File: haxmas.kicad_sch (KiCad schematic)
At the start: 13 parts, among them J1 edge +, J2 b-, J3 edge -, J4 b+, J5 back edge +, J6 back edge -

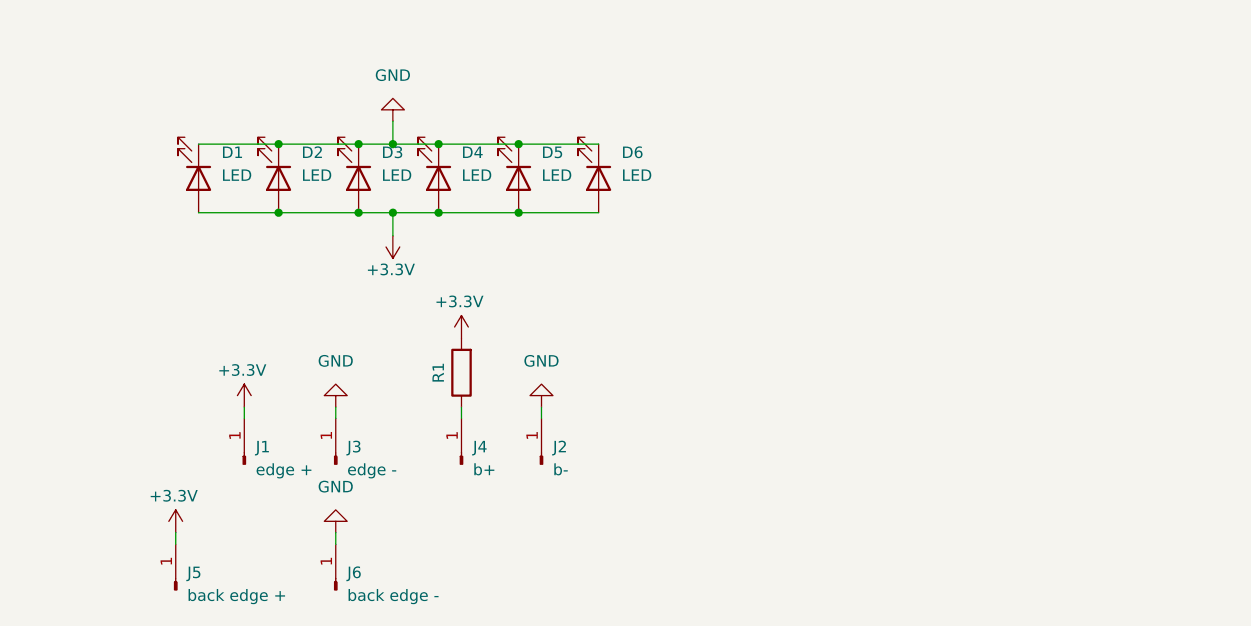
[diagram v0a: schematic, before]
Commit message: feat: add large version
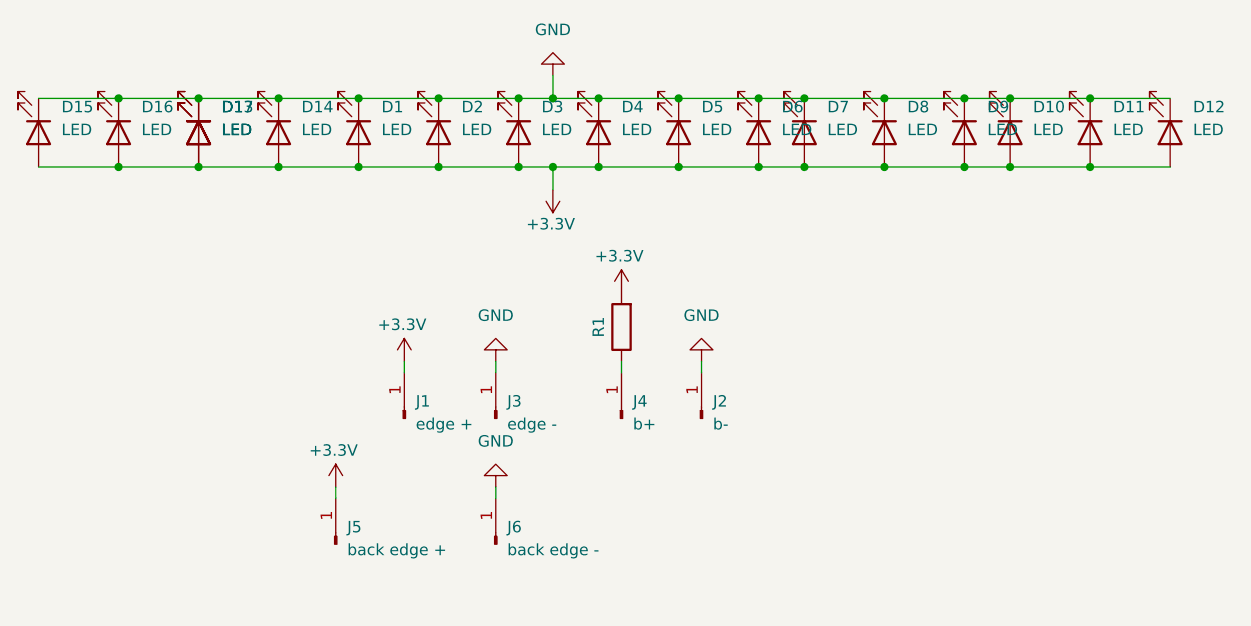
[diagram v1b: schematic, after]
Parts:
- added D10, D11, D12, D13, D14, D15, D16, D17, D7, D8, D9: LED, LED_THT:LED_D3.0mm, symbol Device:LED
- D1, D2, D3, D4, D5, D6: footprint LED_THT:LED_D1.8mm_W3.3mm_H2.4mm -> LED_THT:LED_D3.0mm
- J1, J2, J3, J4, J5, J6: footprint Connector_Wire:SolderWirePad_1x01_SMD_1x2mm -> Connector_Wire:SolderWirePad_1x01_SMD_2x4mm
- R1: footprint Resistor_THT:R_Axial_DIN0204_L3.6mm_D1.6mm_P5.08mm_Horizontal -> Resistor_THT:R_Axial_DIN0204_L3.6mm_D1.6mm_P7.62mm_Horizontal
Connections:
- net +3.3V: now also D10.2 (A), D11.2 (A), D12.2 (A), D13.2 (A), D14.2 (A), D15.2 (A), D16.2 (A), D17.2 (A), D7.2 (A), D8.2 (A), D9.2 (A)
- net GND: now also D10.1 (K), D11.1 (K), D12.1 (K), D13.1 (K), D14.1 (K), D15.1 (K), D16.1 (K), D17.1 (K), D7.1 (K), D8.1 (K), D9.1 (K)
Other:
- moved on the sheet: D1, D2, D3, D4, D5, D6, J1, J2, J3, J4, J5, J6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
